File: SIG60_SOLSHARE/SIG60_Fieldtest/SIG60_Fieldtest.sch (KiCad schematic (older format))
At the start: 2 parts, among them U1 PLC_BOARD

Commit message: cleanup before further PLC development
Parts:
- removed ARDUINO1: ARDUINO_NANO, Modules:Arduino_Nano, symbol ARDUINO_NANO
- added J?: CONN_01X02, symbol CONN_01X02
- added J?: CONN_01X04, symbol CONN_01X04
- added J?: CONN_01X01, symbol CONN_01X01
- added U?: ArduinoProMini, symbol ArduinoProMini
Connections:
- net at U1.1 (GND): now also J?.2 (P2)
- net at U1.2 (VGRID): now also J?.1 (P1)
- net at U1.4 (GND): now also J?.1 (P1), U?.20 (GND)
- net at U1.5 (3.3V): now also U?.22 (VCC)
- net at U1.6 (HDO): now also U?.27 (13)
- net at U1.7 (HDI): now also U?.28 (12)
- net at U1.8 (HDC): now also U?.29 (11)
- net +5V: no longer names the net of U1.3 (VIN)
- net +5V: now also J?.4 (P4)
- new net: J?.1 (P1), U?.30 (10)
- new net: J?.2 (P2), U?.7 (3)
- new net: J?.3 (P3), U?.8 (2)
- no-connect marks 0 -> 22
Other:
- moved on the sheet: U1
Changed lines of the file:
@@
 $EndDescr
 $Comp
-L ARDUINO_NANO ARDUINO1
-U 1 1 5A3D0EC5
-P 2100 1950
-F 0 "ARDUINO1" H 2100 2800 70  0000 C CNN
-F 1 "ARDUINO_NANO" V 2100 1950 70  0000 C CNN
-F 2 "Modules:Arduino_Nano" H 2100 1950 60  0001 C CNN
-F 3 "" H 2100 1950 60  0000 C CNN
-	1    2100 1950
+L PLC_BOARD U1
+U 1 1 5A3BAFAB
+P 3350 4550
+F 0 "U1" V 3350 4200 60  0000 C CNN
+F 1 "PLC_BOARD" H 3350 4900 60  0000 C CNN
+F 2 ".pretty:PLC_BOARD" H 3350 4550 60  0001 C CNN
+F 3 "" H 3350 4550 60  0001 C CNN
+	1    3350 4550
+	0    -1   -1   0
+$EndComp
+$Comp
+L ArduinoProMini U?
+U 1 1 5A5607D3
+P 3550 2900
+F 0 "U?" H 3550 2900 60  0000 C CNN
+F 1 "ArduinoProMini" H 3500 3000 60  0000 C CNN
+F 2 "" H 3550 2900 60  0001 C CNN
+F 3 "" H 3550 2900 60  0001 C CNN
+	1    3550 2900
 	1    0    0    -1
 $EndComp
 $Comp
-L PLC_BOARD U1
-U 1 1 5A3BAFAB
-P 3750 2000
-F 0 "U1" H 3750 1650 60  0000 C CNN
-F 1 "PLC_BOARD" H 3750 2350 60  0000 C CNN
-F 2 ".pretty:PLC_BOARD" H 3750 2000 60  0001 C CNN
-F 3 "" H 3750 2000 60  0001 C CNN
-	1    3750 2000
-	1    0    0    -1
+L CONN_01X02 J?
+U 1 1 5A561214
+P 3350 5450
+F 0 "J?" V 3350 5600 50  0000 C CNN
+F 1 "CONN_01X02" V 3450 5450 50  0000 C CNN
+F 2 "" H 3350 5450 50  0001 C CNN
+F 3 "" H 3350 5450 50  0001 C CNN
+	1    3350 5450
+	0    1    1    0
 $EndComp
+NoConn ~ 3000 2200
+NoConn ~ 3100 2200
+NoConn ~ 3200 2200
+NoConn ~ 3300 2200
+NoConn ~ 3400 2200
+NoConn ~ 3500 2200
+NoConn ~ 3900 2200
+NoConn ~ 4000 2200
+NoConn ~ 4100 2200
+NoConn ~ 4400 2650
+NoConn ~ 4400 3150
+NoConn ~ 4100 3600
+NoConn ~ 3900 3600
+NoConn ~ 3700 3600
+NoConn ~ 3600 3600
+NoConn ~ 3500 3600
+NoConn ~ 3400 3600
 $Comp
-L +5V #PWR?
-U 1 1 5A3BB8FE
-P 2950 950
-F 0 "#PWR?" H 2950 800 50  0001 C CNN
-F 1 "+5V" H 2950 1090 50  0000 C CNN
-F 2 "" H 2950 950 50  0001 C CNN
-F 3 "" H 2950 950 50  0001 C CNN
-	1    2950 950
+L CONN_01X04 J?
+U 1 1 5A5793DC
+P 5600 3950
+F 0 "J?" H 5600 4200 50  0000 C CNN
+F 1 "CONN_01X04" V 5700 3950 50  0000 C CNN
+F 2 "" H 5600 3950 50  0001 C CNN
+F 3 "" H 5600 3950 50  0001 C CNN
+	1    5600 3950
 	1    0    0    -1
 $EndComp
 Wire Wire Line
-	2950 950  2950 1500
+	3300 5250 3300 5050
 Wire Wire Line
-	2950 1500 2700 1500
+	3400 5250 3400 5050
+Wire Wire Line
+	3100 3600 3100 4100
+Wire Wire Line
+	3200 3600 3200 4100
+Wire Wire Line
+	3300 3600 3300 4100
+Wire Wire Line
+	3400 4100 3400 3850
+Wire Wire Line
+	3400 3850 3800 3850
+Wire Wire Line
+	3800 3850 3800 3600
+Wire Wire Line
+	4000 3600 4000 3950
+Wire Wire Line
+	4000 3800 5400 3800
+Wire Wire Line
+	3600 4100 5400 4100
+Wire Wire Line
+	3500 4100 3500 3950
+Wire Wire Line
+	3500 3950 4000 3950
+Connection ~ 4000 3800
+NoConn ~ 4400 3050
+NoConn ~ 4400 2950
+NoConn ~ 4400 2850
+NoConn ~ 4400 2750
+Wire Wire Line
+	5400 3900 5100 3900
+Wire Wire Line
+	5100 3900 5100 1900
+Wire Wire Line
+	5100 1900 3600 1900
+Wire Wire Line
+	3600 1900 3600 2200
+Wire Wire Line
+	5400 4000 4850 4000
+Wire Wire Line
+	4850 4000 4850 2050
+Wire Wire Line
+	4850 2050 3700 2050
+Wire Wire Line
+	3700 2050 3700 2200
+NoConn ~ 3800 2200
 $Comp
-L +5V #PWR?
-U 1 1 5A3BB97E
-P 4650 950
-F 0 "#PWR?" H 4650 800 50  0001 C CNN
-F 1 "+5V" H 4650 1090 50  0000 C CNN
-F 2 "" H 4650 950 50  0001 C CNN
-F 3 "" H 4650 950 50  0001 C CNN
-	1    4650 950
-	1    0    0    -1
+L CONN_01X01 J?
+U 1 1 5A5C9B55
+P 2700 4100
+F 0 "J?" V 2700 4200 50  0000 C CNN
+F 1 "CONN_01X01" V 2800 4100 50  0000 C CNN
+F 2 "" H 2700 4100 50  0001 C CNN
+F 3 "" H 2700 4100 50  0001 C CNN
+	1    2700 4100
+	0    1    1    0
 $EndComp
 Wire Wire Line
-	4200 2250 4650 2250
+	3000 3600 3000 3800
 Wire Wire Line
-	4650 2250 4650 950
+	3000 3800 2700 3800
+Wire Wire Line
+	2700 3800 2700 3900
 $EndSCHEMATC

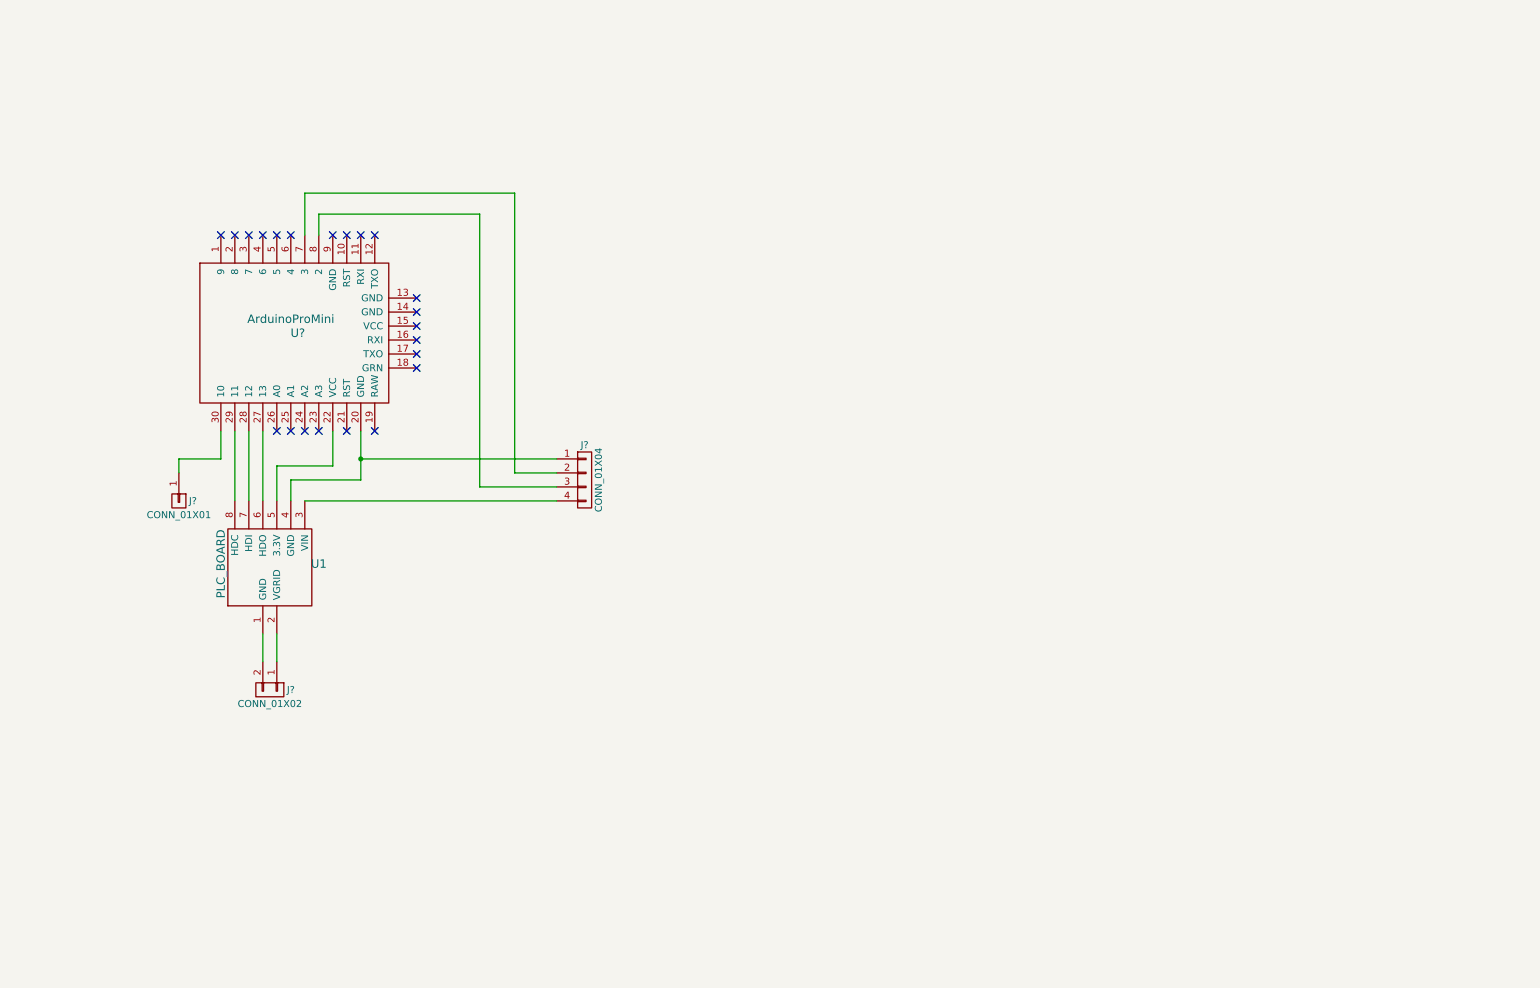
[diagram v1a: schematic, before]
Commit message: Working PLC test console with ping, add device, delete device and list device.
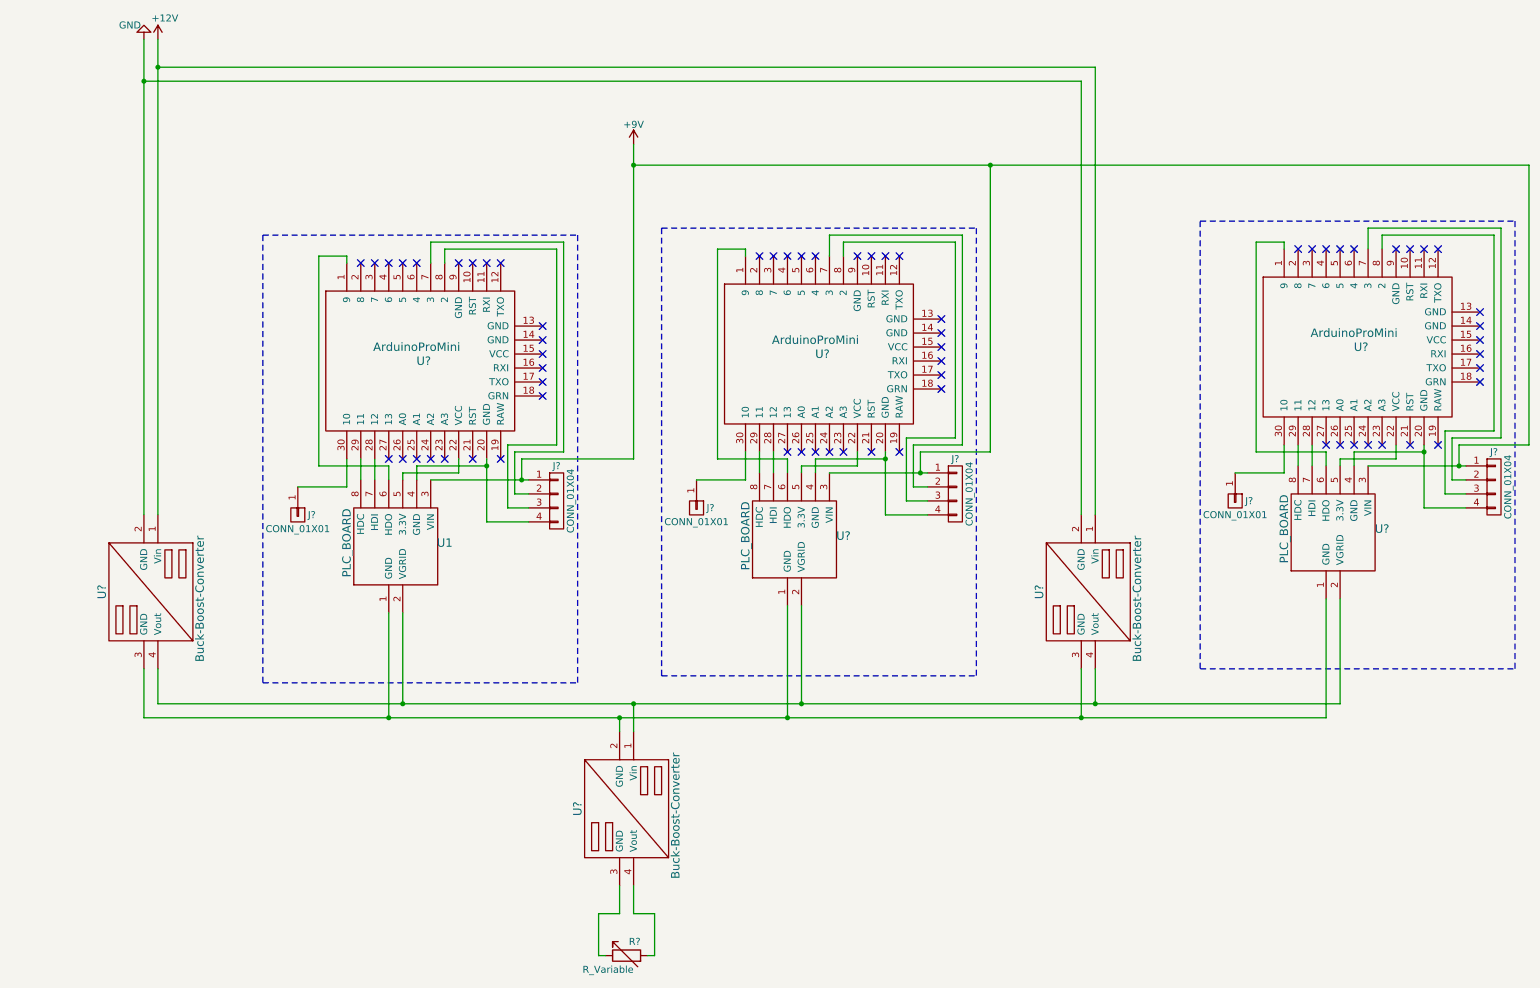
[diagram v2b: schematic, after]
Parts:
- removed J?: CONN_01X02, symbol CONN_01X02
- added J? (x2): CONN_01X04, symbol CONN_01X04
- added J? (x2): CONN_01X01, symbol CONN_01X01
- added R?: R_Variable, symbol R_Variable
- added U? (x3): Buck-Boost-Converter, symbol Buck-Boost-Converter
- added U? (x2): PLC_BOARD, .pretty:PLC_BOARD, symbol PLC_BOARD
- added U? (x2): ArduinoProMini, symbol ArduinoProMini
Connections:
- net at U1.1 (GND): now also U?.1 (GND), U?.1 (GND), U?.2 (GND), U?.3 (GND), U?.3 (GND)
- net at U1.2 (VGRID): now also U?.1 (Vin), U?.2 (VGRID), U?.2 (VGRID), U?.4 (Vout), U?.4 (Vout)
- net at J?.4 (P4): now also U1.4 (GND), U?.20 (GND); no longer U1.3 (VIN)
- net at U1.6 (HDO): now also U?.1 (9); no longer U?.27 (13)
- new net: J?.4 (P4), U?.20 (GND), U?.4 (GND) (x2)
- new net: U?.22 (VCC), U?.5 (3.3V) (x2)
- new net: U?.1 (9), U?.6 (HDO) (x2)
- new net: U?.28 (12), U?.7 (HDI) (x2)
- new net: U?.29 (11), U?.8 (HDC) (x2)
- new net: J?.1 (P1), U?.30 (10) (x2)
- new net: J?.2 (P2), U?.7 (3) (x2)
- new net: J?.3 (P3), U?.8 (2) (x2)
- new net: R?.1, U?.3 (GND)
- new net: R?.2, U?.4 (Vout)
- new net +12V: U?.1 (Vin), U?.1 (Vin)
- new net +9V: J?.1 (P1), J?.1 (P1), J?.1 (P1), U1.3 (VIN), U?.3 (VIN), U?.3 (VIN)
- new net GND: U?.2 (GND), U?.2 (GND)
- no-connect marks 22 -> 66
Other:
- moved on the sheet: J?, U1, U?
